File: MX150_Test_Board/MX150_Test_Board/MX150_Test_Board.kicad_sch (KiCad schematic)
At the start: 0 parts

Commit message: temp commit for branch change
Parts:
- added J1: Conn_02x04_Top_Bottom, symbol Connector_Generic:Conn_02x04_Top_Bottom
- added J2: ~, symbol utsvt_connectors:MX150_02x04_1
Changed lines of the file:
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@@
 	(generator_version "9.0")
 	(paper "A4")
+	(text_box "Vertical: 6, 8, 16, 20\nRight-angle: 8, 16, 20"
+		(exclude_from_sim no)
+		(at 247.65 154.94 0)
+		(size 26.67 5.715)
+		(margins 0.9525 0.9525 0.9525 0.9525)
+		(stroke
+			(width 0)
+			(type solid)
+		)
+		(fill
+			(type none)
+		)
+		(effects
+			(font
+				(size 1.27 1.27)
+			)
+			(justify left top)
+		)
+	)
+	(symbol
+		(lib_id "Connector_Generic:Conn_02x04_Top_Bottom")
+		(at 135.89 73.66 0)
+		(unit 1)
+		(exclude_from_sim no)
+		(in_bom yes)
+		(on_board yes)
+		(dnp no)
+		(fields_autoplaced yes)
+		(property "Reference" "J1"
+			(at 137.16 64.77 0)
+			(effects
+				(font
+					(size 1.27 1.27)
+				)
+			)
+		)
+		(property "Value" "Conn_02x04_Top_Bottom"
+			(at 137.16 67.31 0)
+			(effects
+				(font
+					(size 1.27 1.27)
+				)
+			)
+		)
+		(property "Footprint" ""
+			(at 135.89 73.66 0)
+			(effects
+				(font
+					(size 1.27 1.27)
+				)
+				(hide yes)
+			)
+		)
+		(property "Datasheet" "~"
+			(at 135.89 73.66 0)
+			(effects
+				(font
+					(size 1.27 1.27)
+				)
+				(hide yes)
+			)
+		)
+		(property "Description" "Generic connector, double row, 02x04, top/bottom pin numbering scheme (row 1: 1...pins_per_row, row2: pins_per_row+1 ... num_pins), script generated (kicad-library-utils/schlib/autogen/connector/)"
+			(at 135.89 73.66 0)
+			(effects
+				(font
+					(size 1.27 1.27)
+				)
+				(hide yes)
+			)
+		)
+		(pin "1"
+		)
+		(pin "2"
+		)
+		(pin "3"
+		)
+		(pin "4"
+		)
+		(pin "5"
+		)
+		(pin "6"
+		)
+		(pin "7"
+		)
+		(pin "8"
+		)
+		(instances
+			(project ""
+				(path "/8fe7c543-0639-45c5-bcfa-60af56fd8b6d"
+					(reference "J1")
+					(unit 1)
+				)
+			)
+		)
+	)
+	(symbol
+		(lib_id "utsvt_connectors:MX150_02x04_1")
+		(at 135.89 88.9 0)
+		(unit 1)
+		(exclude_from_sim no)
+		(in_bom yes)
+		(on_board yes)
+		(dnp no)
+		(fields_autoplaced yes)
+		(property "Reference" "J2"
+			(at 135.89 86.36 0)
+			(effects
+				(font
+					(size 1.27 1.27)
+				)
+			)
+		)
+		(property "Value" "~"
+			(at 135.89 88.9 0)
+			(effects
+				(font
+					(size 1.27 1.27)
+				)
+			)
+		)
+		(property "Footprint" ""
+			(at 135.89 88.9 0)
+			(effects
+				(font
+					(size 1.27 1.27)
+				)
+				(hide yes)
+			)
+		)
+		(property "Datasheet" ""
+			(at 135.89 88.9 0)
+			(effects
+				(font
+					(size 1.27 1.27)
+				)
+				(hide yes)
+			)
+		)
+		(property "Description" ""
+			(at 135.89 88.9 0)
+			(effects
+				(font
+					(size 1.27 1.27)
+				)
+				(hide yes)
+			)
+		)
+		(pin "6"
+		)
+		(pin "7"
+		)
+		(pin "3"
+		)
+		(pin "4"
+		)
+		(pin "1"
+		)
+		(pin "2"
+		)
+		(pin "8"
+		)
+		(pin "5"
+		)
+		(instances
+			(project ""
+				(path "/8fe7c543-0639-45c5-bcfa-60af56fd8b6d"
+					(reference "J2")
+					(unit 1)
+				)
+			)
+		)
+	)
 	(sheet_instances
 		(path "/"

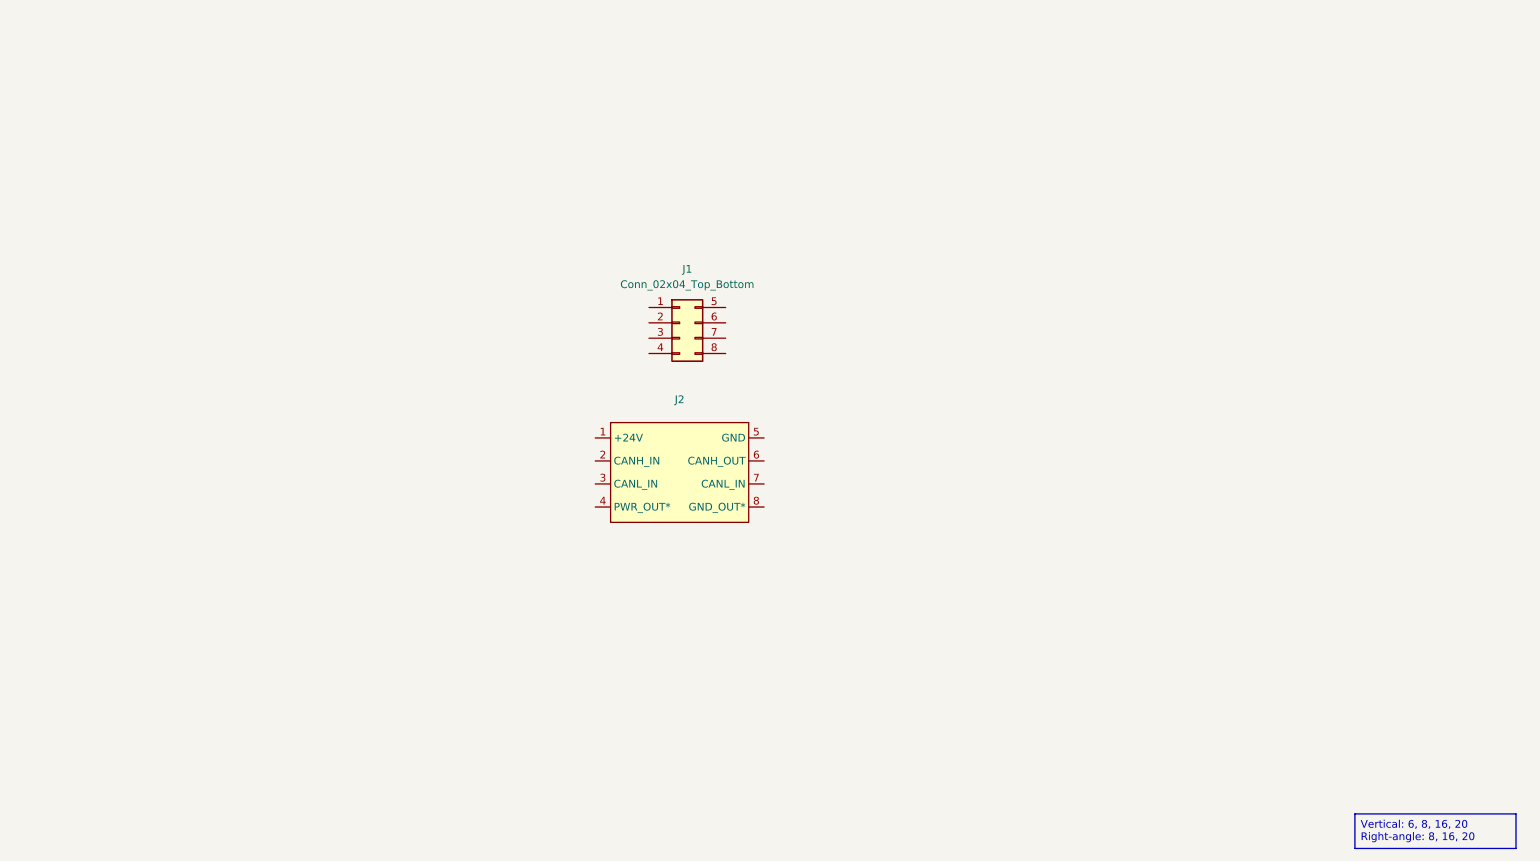
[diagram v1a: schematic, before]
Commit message: fixed symbols + prelim layout
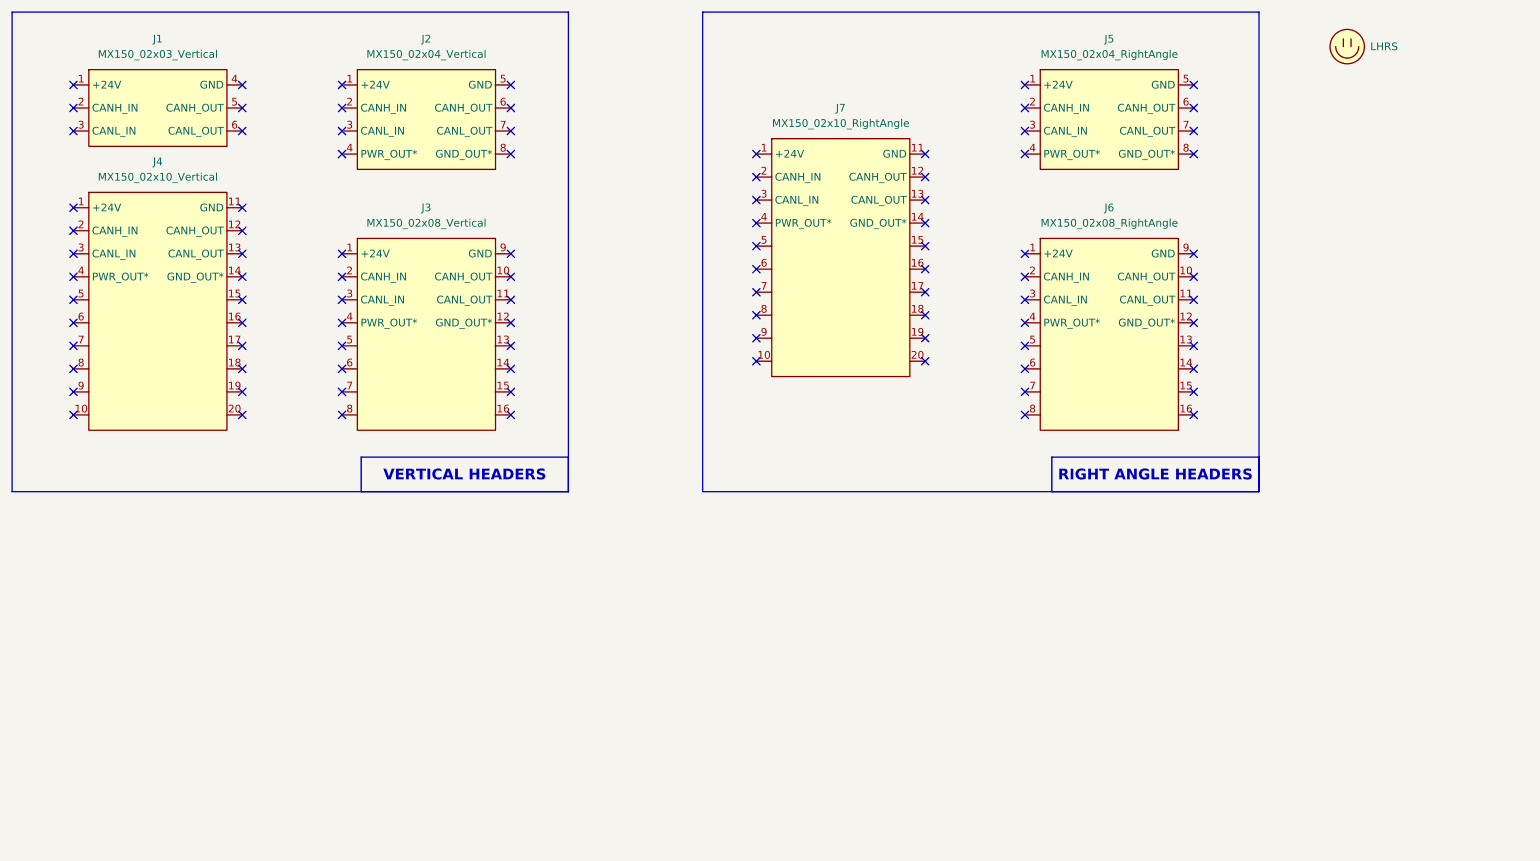
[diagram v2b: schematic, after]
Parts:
- removed J1: Conn_02x04_Top_Bottom, symbol Connector_Generic:Conn_02x04_Top_Bottom
- removed J2: ~, symbol utsvt_connectors:MX150_02x04_1
- added J1: MX150_02x03_Vertical, UTSVT_Connectors:CONN06_0757575131_MOL, symbol utsvt_connectors:MX150_02x03_Vertical
- added J2: MX150_02x04_Vertical, UTSVT_Connectors:CONN_SD-75757-002_2X04_F16p09_MOL, symbol utsvt_connectors:MX150_02x04_Vertical
- added J3: MX150_02x08_Vertical, UTSVT_Connectors:CONN16_0757575481_MOL, symbol utsvt_connectors:MX150_02x08_Vertical
- added J4: MX150_02x10_Vertical, UTSVT_Connectors:CONN_SD-75757-002_2X10_F16p09_MOL, symbol utsvt_connectors:MX150_02x10_Vertical
- added J5: MX150_02x04_RightAngle, UTSVT_Connectors:CONN_SD-75900-001_2X04_MOL, symbol utsvt_connectors:MX150_02x04_RightAngle
- added J6: MX150_02x08_RightAngle, UTSVT_Connectors:CONN_SD-75900-001_2X08_MOL, symbol utsvt_connectors:MX150_02x08_RightAngle
- added J7: MX150_02x10_RightAngle, UTSVT_Connectors:CONN_SD-75900-001_2X10_MOL, symbol utsvt_connectors:MX150_02x10_RightAngle
- added LOGO1: LHRS, UTSVT_Logos:LHRs_LOGO, symbol utsvt_misc:Logo_Placeholder
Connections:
- no-connect marks 0 -> 94

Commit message: updated symbols
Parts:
- J1: P/N (none) -> 757575131
- J2: P/N (none) -> 757575141
- J3: P/N (none) -> 757575481
- J4: P/N (none) -> 757575101
- J5: P/N (none) -> 759001141
- J6: P/N (none) -> 759001181
- J7: P/N (none) -> 759001101
